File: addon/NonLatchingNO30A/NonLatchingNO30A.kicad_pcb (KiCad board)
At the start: 4 copper layers, 153 x 114 mm, 27 parts, among them J101 Conn_02x20_Odd_Even Header, J102 TBP01R2W-508-16BE, J103 TBP01R2W-508-16BE, K101 ALFG2PF121, K102 ALFG2PF121, K103 ALFG2PF121, K104 ALFG2PF121, K105 ALFG2PF121, K106 ALFG2PF121, K107 ALFG2PF121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

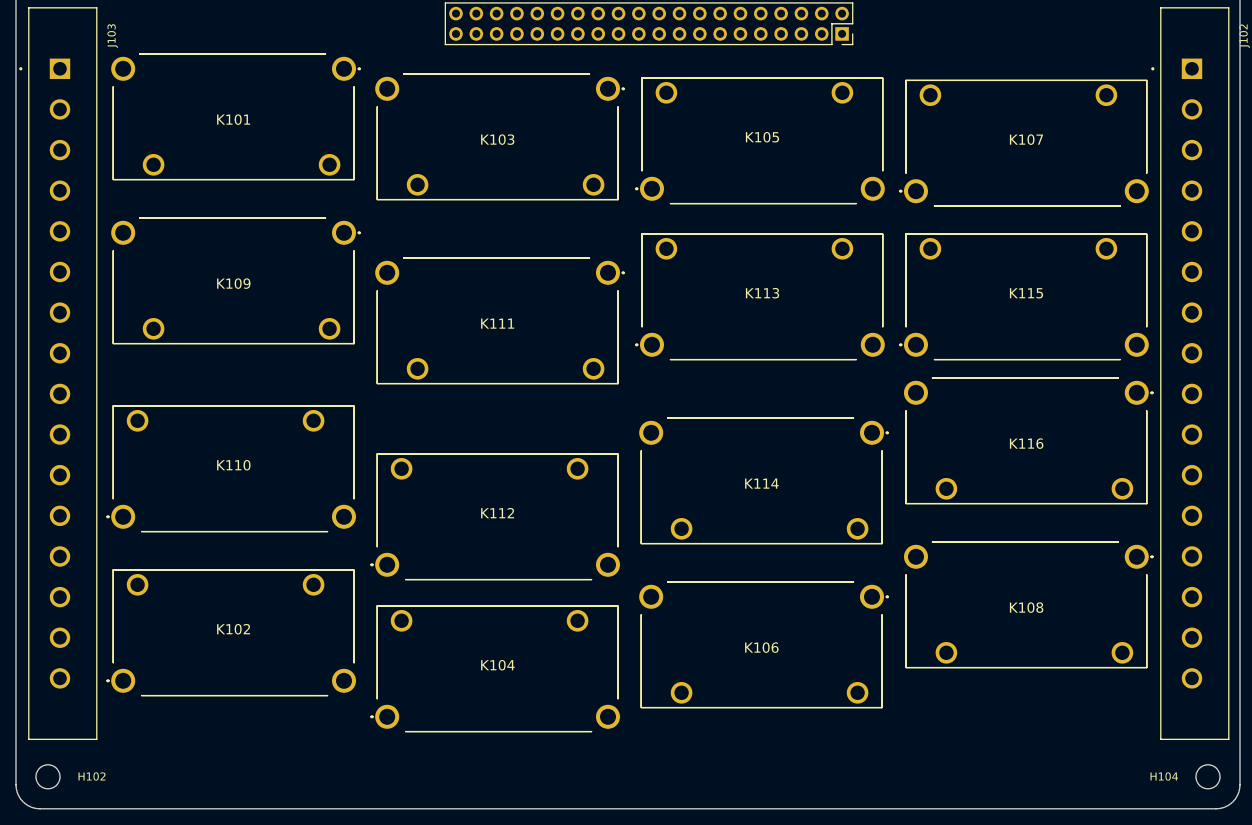
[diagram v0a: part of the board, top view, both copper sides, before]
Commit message: Need to trim down 30A addon board traces to 2.7
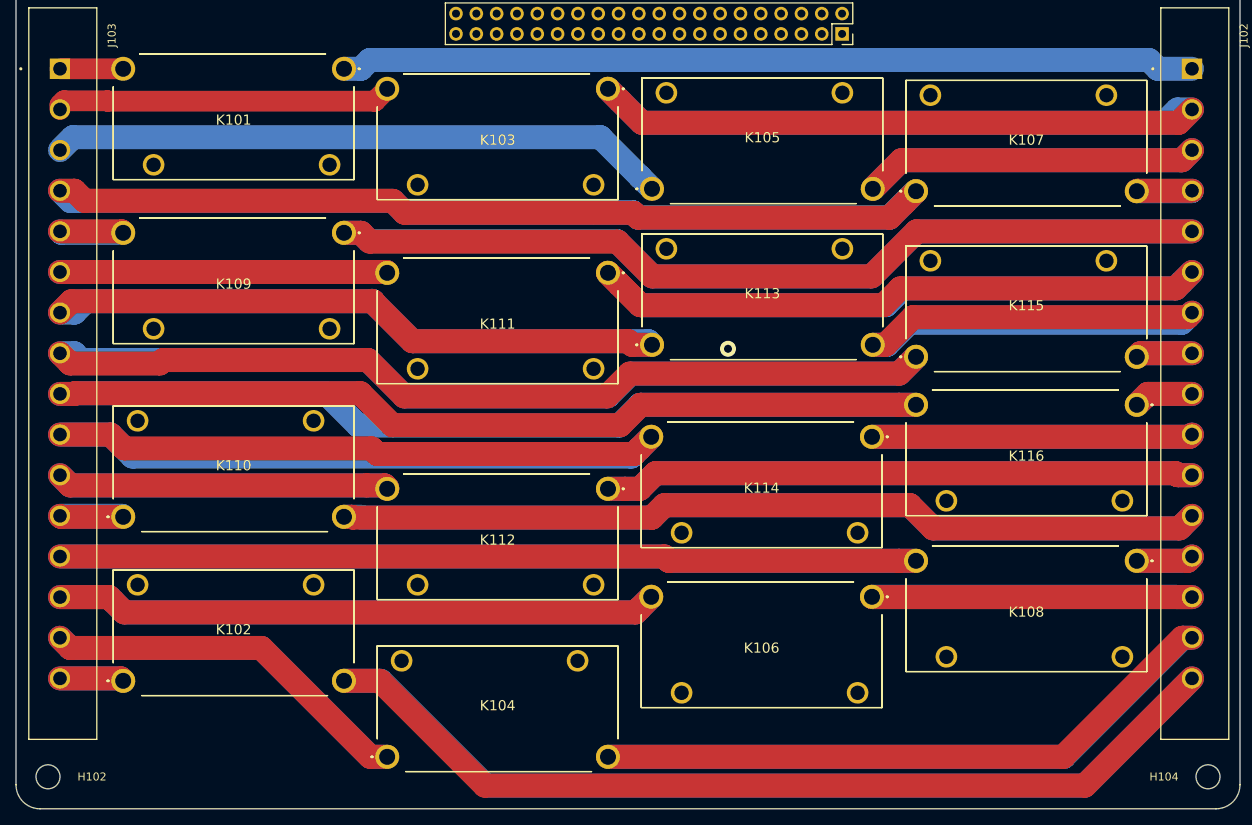
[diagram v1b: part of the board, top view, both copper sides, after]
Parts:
- moved K112 29.2 mm to (124.0, 97.0), turned to 180 degrees
- moved K104 5.00 mm to (96.4, 130.5)
- moved K115 1.50 mm to (162.5, 80.5)
- moved K116 1.50 mm to (190.1, 86.5)
- moved K108 0.50 mm to (190.1, 106.0)
- moved K114 0.50 mm to (157.0, 90.5)
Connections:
- K112 pad 1: Net-(J103-Pad11) -> Net-(J102-Pad11)
- K112 pad 2: Net-(J102-Pad11) -> Net-(J103-Pad11)
- K112 pad 3: /K11_COIL_ON -> GND
- K112 pad 4: GND -> /K11_COIL_ON
- K115 pad 1: Net-(J102-Pad8) -> Net-(J103-Pad8)
- K115 pad 2: Net-(J103-Pad8) -> Net-(J102-Pad8)
- K115 pad 3: GND -> /K8_COIL_ON
- K115 pad 4: /K8_COIL_ON -> GND
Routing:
- net Net-(J103-Pad4): track 0.00 -> 286.6 mm
- net Net-(J102-Pad16): track 0.00 -> 234.0 mm
- net Net-(J103-Pad8): track 0.00 -> 222.9 mm
- net Net-(J102-Pad5): track 0.00 -> 221.2 mm
- net Net-(J103-Pad9): track 0.00 -> 219.5 mm
- net Net-(J102-Pad12): track 0.00 -> 217.1 mm
- net Net-(J103-Pad13): track 0.00 -> 214.4 mm
- net Net-(J102-Pad6): track 0.00 -> 158.5 mm
- net Net-(J102-Pad15): track 0.00 -> 158.3 mm
- net /K13_COIL_ON: track 0.00 -> 156.8 mm
- net Net-(J103-Pad7): track 0.00 -> 154.0 mm
- net Net-(J103-Pad10): track 0.00 -> 151.9 mm
- net Net-(J103-Pad14): track 0.00 -> 151.0 mm
- net Net-(J102-Pad2): track 0.00 -> 150.9 mm
- net Net-(J102-Pad11): track 0.00 -> 147.8 mm
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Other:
- net class Default: via_dia 0.8 -> 1
- rule trace_min: 0.5 -> 1
- rule via_min_size: 0.4 -> 1
- board text added: "4 Layers (6oz -1oz - 1oz - 6oz)"
- board text added: "6oz B.Cu"
- board text added: "6oz F.Cu"
- board text removed: "13oz B.Cu"
- board text removed: "13oz F.Cu"
- board text removed: "4 Layers (13oz -1oz - 1oz - 13oz)"

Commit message: Fix readme
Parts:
- moved LOGO101 3.98 mm to (76.5, 33.9)
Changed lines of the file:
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@@
   )
   (setup
-    (last_trace_width 2.6)
+    (last_trace_width 1)
     (user_trace_width 2)
     (user_trace_width 2.6)
@@
   )
   (module Symbol:KiCad-Logo2_20mm_SilkScreen (layer B.Cu)
-    (at 73 32)
+    (at 76.5 33.9)
     (descr "KiCad Logo")
     (tags "Logo KiCad")
@@
   )
   (gr_line (start 160.6 191.1) (end 124.6 191.1) (layer F.Fab) (width 0.15))
-  (gr_text https://github.com/antevens/boatcontrol (at 135 25.5 180) (layer B.SilkS)
+  (gr_text https://github.com/antevens/boatcontrol (at 144.3 25.5 180) (layer B.SilkS)
     (effects (font (size 1.5 1.5) (thickness 0.3)) (justify mirror))
   )
-  (gr_text bc@ant.st (at 102.5 25.5 180) (layer B.SilkS)
+  (gr_text bc@ant.st (at 111.8 25.5 180) (layer B.SilkS)
     (effects (font (size 1.5 1.5) (thickness 0.3)) (justify mirror))
   )

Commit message: Wrap up non-latching
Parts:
- G101: moved to B.Cu
- LOGO101: footprint Symbol:KiCad-Logo2_20mm_SilkScreen -> Symbol:KiCad-Logo2_12mm_SilkScreen
- moved G102 364.8 mm to (75.0, 128.0)
- moved G101 224.1 mm to (127.0, 80.0)
- moved K106 5.00 mm to (157.0, 115.5)
- moved K114 3.50 mm to (157.0, 94.0)
- moved LOGO101 2.15 mm to (75.5, 32.0)
- moved K104 1.00 mm to (96.4, 129.5)
- moved K108 0.50 mm to (190.1, 106.5)
- moved K112 0.50 mm to (124.0, 97.5)
- moved K113 0.50 mm to (129.5, 79.5)
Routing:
- net GND: track 50.8 -> 602.0 mm
- net Net-(J102-Pad5): track 221.2 -> 0.00 mm
- net Net-(J102-Pad1): track 106.9 -> 236.9 mm
- net /K2_COIL_ON: track 77.6 -> 164.4 mm, vias 1 -> 0
- net Net-(J103-Pad3): track 77.3 -> 155.3 mm
- net Net-(J103-Pad4): track 286.6 -> 220.1 mm
- net /K8_COIL_ON: track 82.5 -> 137.9 mm
- net Net-(J103-Pad2): track 42.3 -> 83.9 mm
- net /K5_COIL_ON: track 124.9 -> 103.7 mm
- net /K9_COIL_ON: track 106.8 -> 93.6 mm
- net /K12_COIL_ON: track 69.2 -> 80.8 mm
- net /K11_COIL_ON: track 82.3 -> 91.4 mm
- net Net-(J103-Pad13): track 214.4 -> 222.9 mm
- net Net-(J103-Pad1): track 7.90 -> 15.8 mm
- net Net-(J103-Pad8): track 222.9 -> 230.6 mm
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- added copper zone on B.Cu, net Net-(J102-Pad5)
- added copper zone on F.Cu, net Net-(J102-Pad5)
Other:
- board text added: "16 x 30A NO"
- board text added: "Boatcontrol Addon Board"
- board text added: "Revision 3 {HASH}"

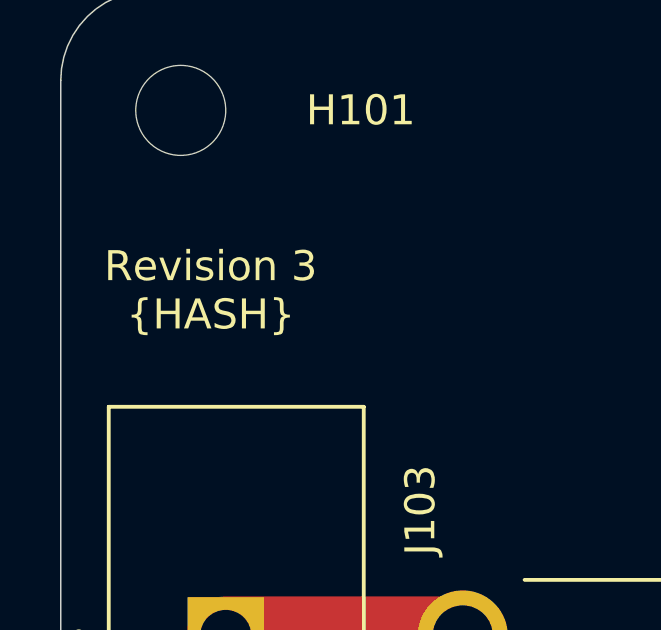
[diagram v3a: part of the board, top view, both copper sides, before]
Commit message: Revision 2 of non-latching
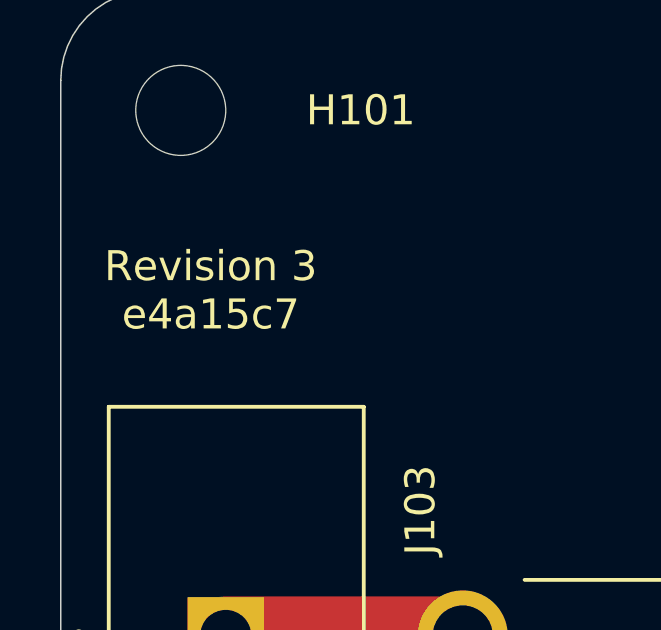
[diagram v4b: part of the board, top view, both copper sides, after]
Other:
- board text added: "Revision 3 e4a15c7"
- board text removed: "Revision 3 {HASH}"
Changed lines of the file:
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@@
     (comment 2 https://github.com/antevens/boatcontrol/addon/CommonCathode60A)
     (comment 3 a@ant.st)
+    (comment 4 e4a15c7d5454532087f6000c5f26d57cda012915)
   )
   (layers
@@
     (effects (font (size 4 4) (thickness 0.5)))
   )
-  (gr_text "Revision 3\n{HASH}" (at 55 33) (layer F.SilkS)
+  (gr_text "Revision 3\ne4a15c7" (at 55 33) (layer F.SilkS)
     (effects (font (size 1 1) (thickness 0.2)))
   )

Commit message: Prototype time
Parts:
- moved G102 2.50 mm to (77.5, 128.0)
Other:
- board text added: "#1"
- board text added: "#16"
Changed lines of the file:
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@@
   (general
     (thickness 1.6)
-    (drawings 72)
+    (drawings 76)
     (tracks 499)
     (zones 0)
@@
   (module BoatControl:CUI_TBP01R2W-508-16BE (layer F.Cu)
     (at 55.5 44.5 270)
-    (fp_text reference J103 (at -4.175 -6.489 90) (layer F.SilkS)
+    (fp_text reference J103 (at -8.5 -6 90) (layer F.SilkS)
       (effects (font (size 1 1) (thickness 0.2)))
     )
@@
   )
   (module BoatControl:Ant_Logo_SilkScreen (layer F.Cu)
-    (at 75 128)
+    (at 77.5 128)
     (attr virtual)
     (fp_text reference G102 (at 0 5.08) (layer F.SilkS) hide
@@
     (pad 1 np_thru_hole circle (at 0 0) (size 3 3) (drill 3) (layers *.Cu *.Mask))
   )
+  (gr_text "#16" (at 189 126.25) (layer F.SilkS)
+    (effects (font (size 2 2) (thickness 0.2)))
+  )
+  (gr_text "#16" (at 63.5 126.5) (layer F.SilkS)
+    (effects (font (size 2 2) (thickness 0.2)))
+  )
+  (gr_text "#1" (at 191 42) (layer F.SilkS)
+    (effects (font (size 2 2) (thickness 0.2)))
+  )
+  (gr_text "#1" (at 62.5 40) (layer F.SilkS)
+    (effects (font (size 2 2) (thickness 0.2)))
+  )
   (dimension 114 (width 0.15) (layer F.Fab)
